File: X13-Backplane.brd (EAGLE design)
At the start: 101.6 x 139.3 mm, 38 parts, among them J1 PXC-PTSM-04-RA-1778641, J2 284512-4, J3 284512-8, J4 PXC-PTSM-04-RA-1778641, J5 PXC-PTSM-04-RA-1778641, J6 284512-4, J8 284512-8, T1 284512-3, T2 284512-3, T3 284512-3, T4 284512-3, T5 284512-3, T6 284512-3, T7 284512-3, T8 284512-3

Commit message: updated mux
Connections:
- removed net SWCLK_4: MUX.11
- removed net SWDIO_4: MUX.4
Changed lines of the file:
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@@
 <wire x1="15.08125" y1="51.435" x2="15.08125" y2="48.5648" width="0.2032" layer="1"/>
-</signal>
-<signal name="SWDIO_4">
-<contactref element="MUX" pad="4"/>
-</signal>
-<signal name="SWCLK_4">
-<contactref element="MUX" pad="11"/>
 </signal>
 <signal name="T1_PHS1">

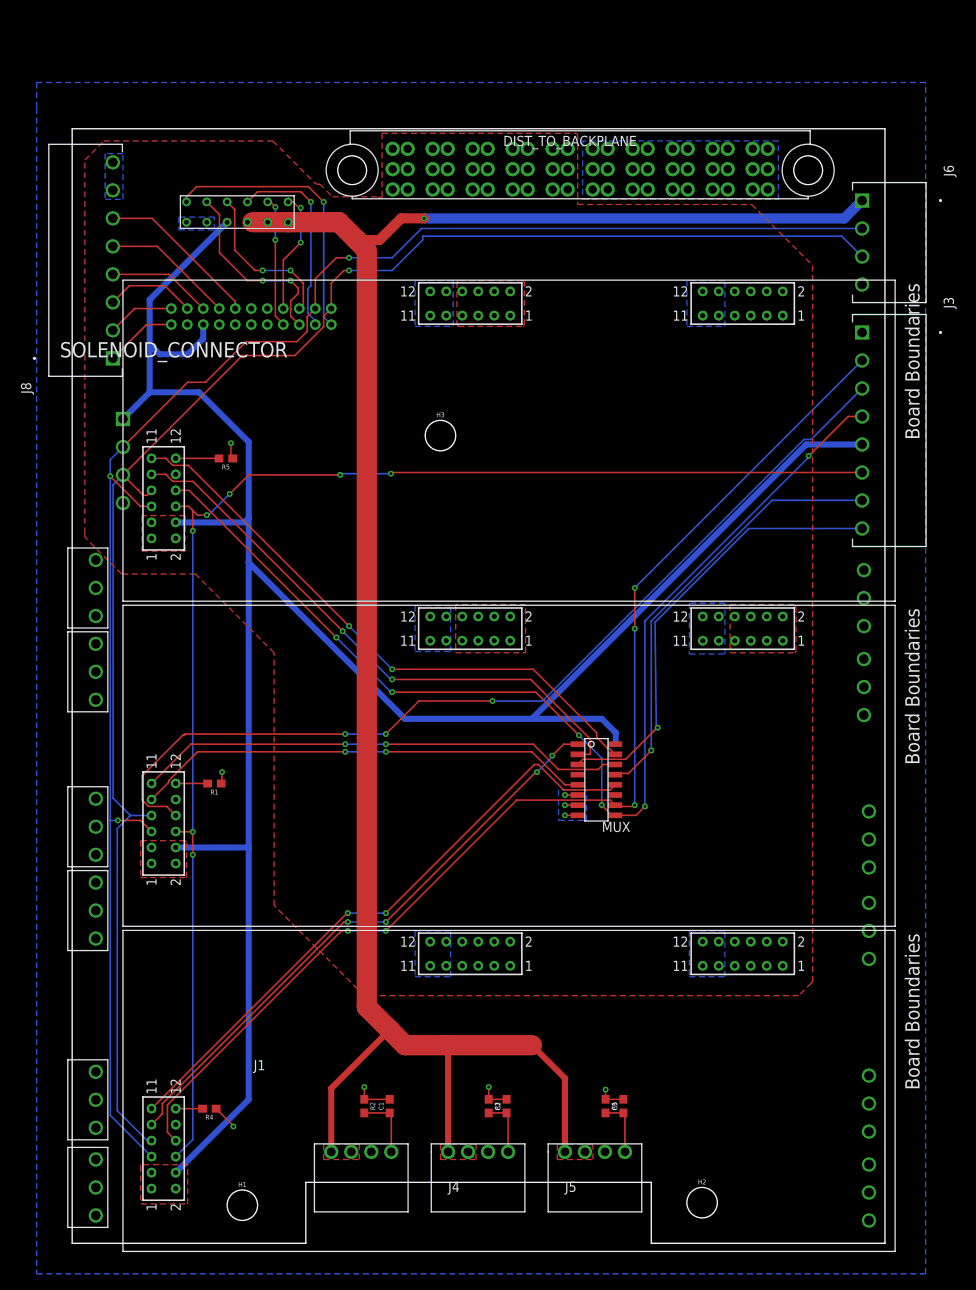
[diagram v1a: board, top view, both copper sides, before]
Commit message: updated 5v trace
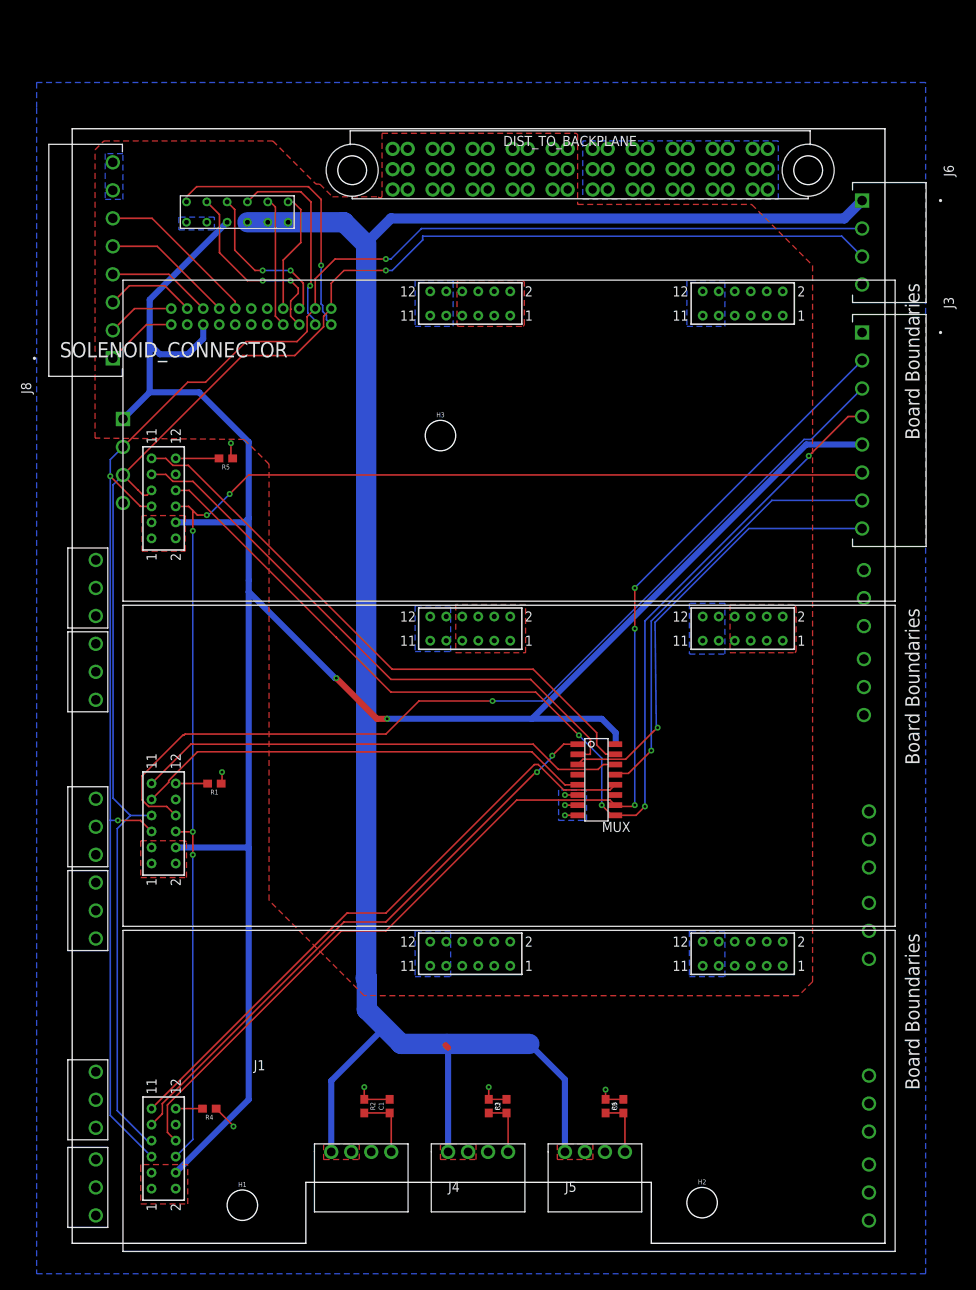
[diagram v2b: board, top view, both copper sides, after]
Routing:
- net 3.3V: track 279.8 -> 278.3 mm, vias 0 -> 2
- net SWCLK_3: track 73.6 -> 74.2 mm, vias 2 -> 0
- net C2_2: track 15.7 -> 15.3 mm, vias 2 -> 0
- net 5V: track 245.0 -> 244.8 mm, vias 1 -> 0
- net PROG_3: vias 6 -> 4
- net PROG_1: vias 5 -> 3
- net NRST: vias 7 -> 5
- net SWCLK_1: vias 2 -> 0
- net PROG_2: vias 3 -> 1
- net SWCLK_2: vias 2 -> 0
- net SWDIO_3: vias 2 -> 0
- net SWDIO_2: vias 2 -> 0
- net SWDIO_1: vias 4 -> 2
- net C2_1: vias 2 -> 0

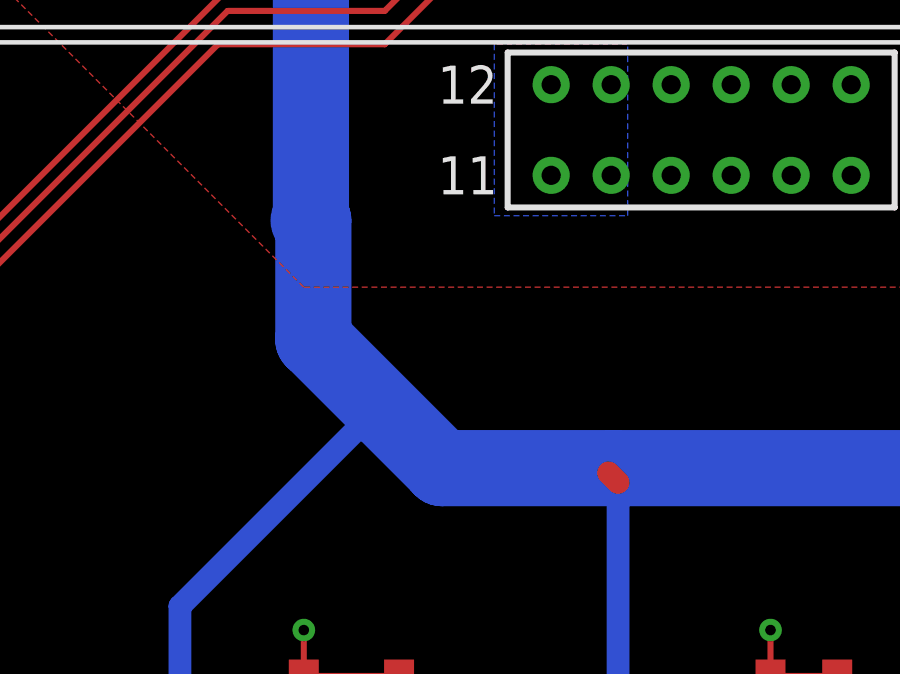
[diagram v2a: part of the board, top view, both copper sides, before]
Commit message: updated 5v trace
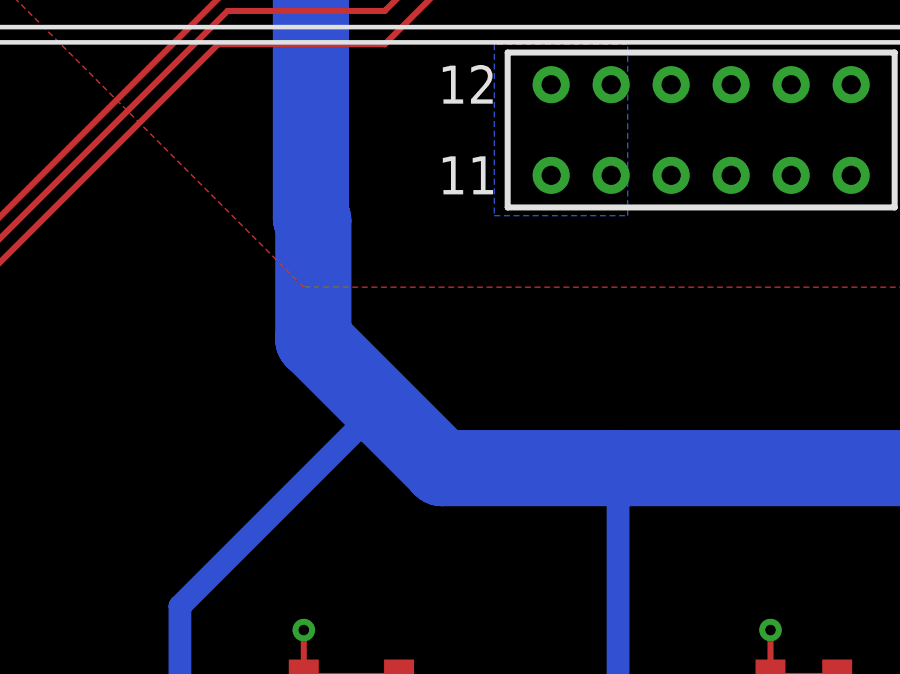
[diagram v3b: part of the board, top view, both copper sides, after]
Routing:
- net 5V: track 244.8 -> 244.2 mm
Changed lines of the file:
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@@
 <vertex x="65.0875" y="12.3825"/>
 </polygon>
-<wire x1="46.6725" y1="24.765" x2="46.99" y2="24.4475" width="0.762" layer="1"/>
 <wire x1="96.50875" y1="128.11125" x2="98.7425" y2="130.345" width="1.27" layer="16"/>
 <wire x1="21.9075" y1="127.635" x2="33.9725" y2="127.635" width="2.54" layer="16"/>
@@
 <wire x1="39.84625" y1="128.11125" x2="96.50875" y2="128.11125" width="1.27" layer="16"/>
 <wire x1="36.750625" y1="125.015625" x2="36.750625" y2="33.258125" width="2.54" layer="16"/>
-<wire x1="36.67125" y1="33.17875" x2="36.750625" y2="33.258125" width="2.54" layer="16"/>
 <wire x1="36.750625" y1="33.258125" x2="36.83" y2="33.17875" width="2.54" layer="16"/>
 <wire x1="36.83" y1="33.17875" x2="36.83" y2="29.21" width="2.54" layer="16"/>
@@
 <wire x1="24.4475" y1="127.635" x2="26.9875" y2="127.635" width="0" layer="19" extent="1-1"/>
 <wire x1="21.9075" y1="127.635" x2="24.4475" y2="127.635" width="0" layer="19" extent="1-1"/>
-<wire x1="38.25875" y1="26.19375" x2="36.67125" y2="33.17875" width="0" layer="19" extent="16-16"/>
-<wire x1="46.6725" y1="24.765" x2="38.25875" y2="26.19375" width="0" layer="19" extent="1-16"/>
+<wire x1="64.095" y1="11.43" x2="61.595" y2="11.43" width="0" layer="19" extent="1-1"/>
+<wire x1="49.49" y1="11.43" x2="46.99" y2="11.43" width="0" layer="19" extent="1-1"/>
+<wire x1="34.885" y1="11.43" x2="46.99" y2="11.43" width="0" layer="19" extent="1-1"/>
+<wire x1="32.385" y1="11.43" x2="34.885" y2="11.43" width="0" layer="19" extent="1-1"/>
 </signal>
 <signal name="12V">

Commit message: updated spacing on parts
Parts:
- moved MC2 1.91 mm to (100.8, 67.6)
- moved MC1 1.12 mm to (100.8, 79.5)
- moved T5 0.95 mm to (0.95, 40.6)
- moved T7 0.79 mm to (0.95, 70.6)
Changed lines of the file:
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@@
 <attribute name="VALUE" x="94.0925" y="118.3" size="1.27" layer="27" rot="R270"/>
 </element>
-<element name="MC1" library="ThrusterConnector" package="284512-3" value="284512-3" x="100.965" y="80.645" smashed="yes" rot="MR180"/>
-<element name="MC2" library="ThrusterConnector" package="284512-3" value="284512-3" x="100.965" y="69.5325" smashed="yes" rot="MR180"/>
+<element name="MC1" library="ThrusterConnector" package="284512-3" value="284512-3" x="100.80625" y="79.53375" smashed="yes" rot="MR180"/>
+<element name="MC2" library="ThrusterConnector" package="284512-3" value="284512-3" x="100.80625" y="67.6275" smashed="yes" rot="MR180"/>
 <element name="MC3" library="ThrusterConnector" package="284512-3" value="284512-3" x="101.6" y="50.4825" smashed="yes" rot="MR180"/>
 <element name="MC4" library="ThrusterConnector" package="284512-3" value="284512-3" x="101.6" y="39.0525" smashed="yes" rot="MR180"/>
@@
 <element name="T3" library="ThrusterConnector" package="284512-3" value="284512-3" x="0.9525" y="6.985" smashed="yes" rot="R180"/>
 <element name="T4" library="ThrusterConnector" package="284512-3" value="284512-3" x="0.9525" y="17.93875" smashed="yes" rot="R180"/>
-<element name="T5" library="ThrusterConnector" package="284512-3" value="284512-3" x="0.9525" y="41.5925" smashed="yes" rot="R180"/>
+<element name="T5" library="ThrusterConnector" package="284512-3" value="284512-3" x="0.9525" y="40.64" smashed="yes" rot="R180"/>
 <element name="T6" library="ThrusterConnector" package="284512-3" value="284512-3" x="0.9525" y="52.07" smashed="yes" rot="R180"/>
-<element name="T7" library="ThrusterConnector" package="284512-3" value="284512-3" x="0.9525" y="71.4375" smashed="yes" rot="R180"/>
+<element name="T7" library="ThrusterConnector" package="284512-3" value="284512-3" x="0.9525" y="70.64375" smashed="yes" rot="R180"/>
 <element name="T8" library="ThrusterConnector" package="284512-3" value="284512-3" x="0.9525" y="81.915" smashed="yes" rot="R180"/>
 <element name="J1" library="Phoenix Contact PTSM-04-V-1778573" package="PXC-PTSM-04-RA-1778641" value="PXC-PTSM-04-RA-1778641" x="32.385" y="11.43" smashed="yes">

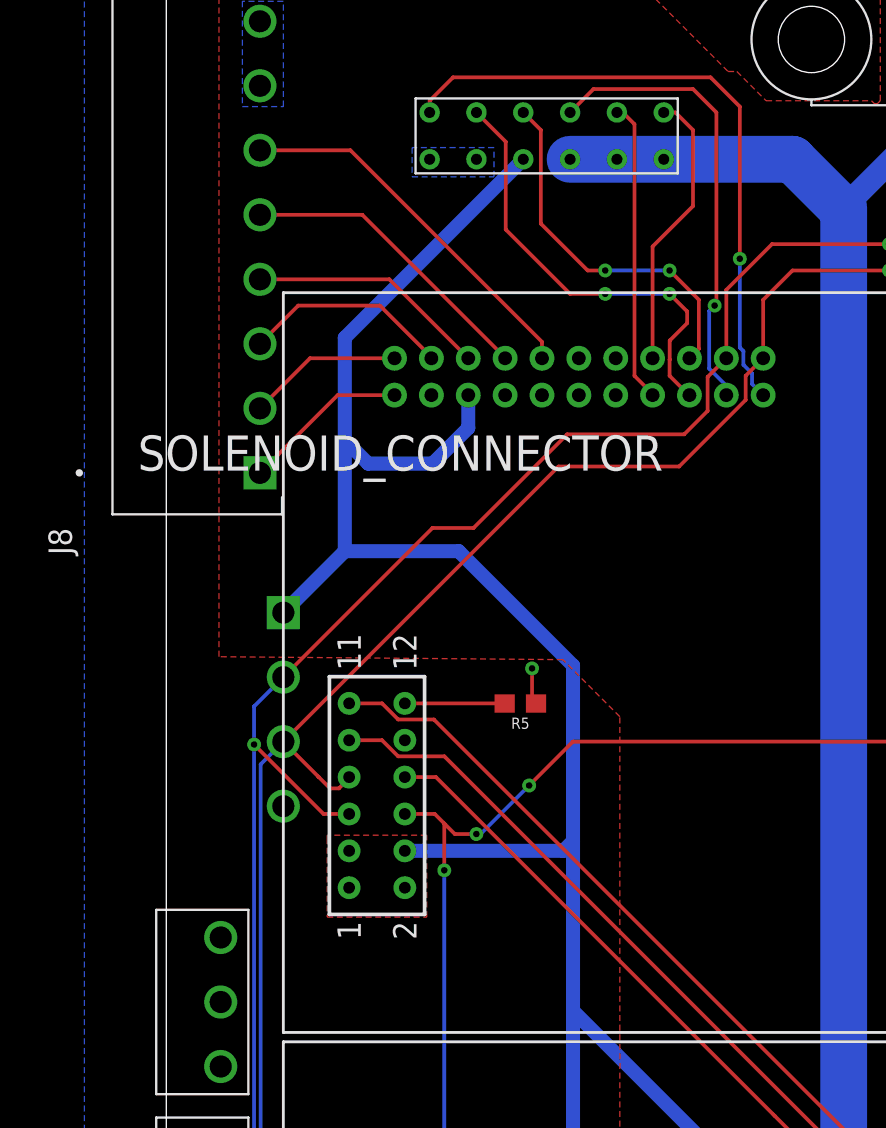
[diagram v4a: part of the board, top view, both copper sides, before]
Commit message: Placed Solenoid Connector and schematic pinout
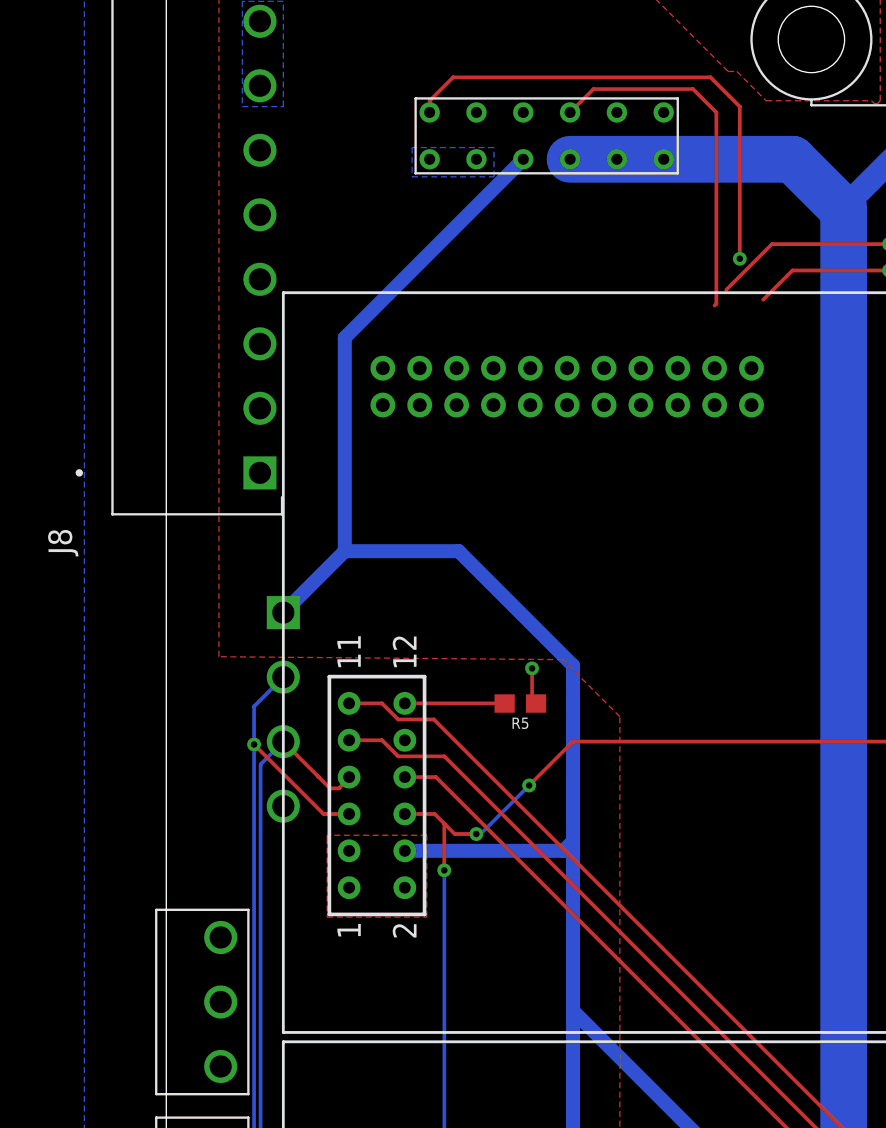
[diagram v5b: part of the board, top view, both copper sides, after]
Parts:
- removed SOLENOID_CONNECTOR: BKP-TO-SOL, Solenoid Connector (backplane side):BKP-TO-SOL_TMM-111-01-T-D
- added U$4: BKP-TO-SOL, Solenoid Connector (backplane side):BKP-TO-SOL_TMM-111-01-T-D
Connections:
- new net DATA1: U$4.22
- net 12V: now also U$4.11; no longer SOLENOID_CONNECTOR.11
- net 3.3V: now also U$4.4; no longer SOLENOID_CONNECTOR.6
- net ALERT_1: now also U$4.18; no longer SOLENOID_CONNECTOR.18
- net ALERT_2: now also U$4.17; no longer SOLENOID_CONNECTOR.17
- net C2_1: now also U$4.16; no longer SOLENOID_CONNECTOR.16
- net C2_2: now also U$4.15; no longer SOLENOID_CONNECTOR.15
- net CAN_H: now also U$4.19; no longer SOLENOID_CONNECTOR.19
- net CAN_L: now also U$4.21; no longer SOLENOID_CONNECTOR.21
- net CLK: now also U$4.20; no longer SOLENOID_CONNECTOR.20
- net DATA: no longer SOLENOID_CONNECTOR.22
- net GND: now also U$4.10, U$4.12, U$4.6, U$4.8; no longer SOLENOID_CONNECTOR.10, SOLENOID_CONNECTOR.12, SOLENOID_CONNECTOR.4, SOLENOID_CONNECTOR.8
- net MC1_PHS1: now also MC1.1; no longer MC1.P$1
- net MC1_PHS2: now also MC1.2; no longer MC1.P$2
- net MC1_PHS3: now also MC1.3; no longer MC1.P$3
- net MC2_PHS1: now also MC2.1; no longer MC2.P$1
- net MC2_PHS2: now also MC2.2; no longer MC2.P$2
- net MC2_PHS3: now also MC2.3; no longer MC2.P$3
- net MC3_PHS1: now also MC3.1; no longer MC3.P$1
- net MC3_PHS2: now also MC3.2; no longer MC3.P$2
- net MC3_PHS3: now also MC3.3; no longer MC3.P$3
- net MC4_PHS1: now also MC4.1; no longer MC4.P$1
- net MC4_PHS2: now also MC4.2; no longer MC4.P$2
- net MC4_PHS3: now also MC4.3; no longer MC4.P$3
- net NRST: now also U$4.13
- net SOL1_1: now also U$4.2; no longer SOLENOID_CONNECTOR.2
- net SOL2_1: now also U$4.1; no longer SOLENOID_CONNECTOR.1
- net SOL3_1: now also U$4.3; no longer SOLENOID_CONNECTOR.3
- net SOL4_1: now also U$4.5; no longer SOLENOID_CONNECTOR.5
- net SOL5_1: now also U$4.7; no longer SOLENOID_CONNECTOR.7
- net SOL6_1: now also U$4.9; no longer SOLENOID_CONNECTOR.9
- net T1_PHS1: now also T1.1; no longer T1.P$1
- net T1_PHS2: now also T1.2; no longer T1.P$2
- net T1_PHS3: now also T1.3; no longer T1.P$3
- net T2_PHS1: now also T2.1; no longer T2.P$1
- net T2_PHS2: now also T2.2; no longer T2.P$2
- net T2_PHS3: now also T2.3; no longer T2.P$3
- net T3_PHS1: now also T3.1; no longer T3.P$1
- net T3_PHS2: now also T3.2; no longer T3.P$2
- net T3_PHS3: now also T3.3; no longer T3.P$3
- net T4_PHS1: now also T4.1; no longer T4.P$1
- net T4_PHS2: now also T4.2; no longer T4.P$2
- net T4_PHS3: now also T4.3; no longer T4.P$3
- net T5_PHS1: now also T5.1; no longer T5.P$1
- net T5_PHS2: now also T5.2; no longer T5.P$2
- net T5_PHS3: now also T5.3; no longer T5.P$3
- net T6_PHS1: now also T6.1; no longer T6.P$1
- net T6_PHS2: now also T6.2; no longer T6.P$2
- net T6_PHS3: now also T6.3; no longer T6.P$3
- net T7_PHS1: now also T7.1; no longer T7.P$1
- net T7_PHS2: now also T7.2; no longer T7.P$2
- net T7_PHS3: now also T7.3; no longer T7.P$3
- net T8_PHS1: now also T8.1; no longer T8.P$1
- net T8_PHS2: now also T8.2; no longer T8.P$2
- net T8_PHS3: now also T8.3; no longer T8.P$3
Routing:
- net CAN_L: track 203.7 -> 165.1 mm
- net CAN_H: track 210.9 -> 175.0 mm
- net ALERT_1: track 24.1 -> 0.00 mm, vias 2 -> 0
- net SOL6_1: track 20.5 -> 0.00 mm
- net ALERT_2: track 20.1 -> 0.00 mm, vias 2 -> 0
- net SOL5_1: track 16.5 -> 0.00 mm
- net C2_1: track 16.3 -> 0.00 mm
- net C2_2: track 15.3 -> 0.00 mm
- net SOL4_1: track 13.1 -> 0.00 mm
- net SOL3_1: track 11.4 -> 0.00 mm
- net 3.3V: track 278.3 -> 268.5 mm
- net SOL1_1: track 9.05 -> 0.00 mm
- net SOL2_1: track 8.43 -> 0.00 mm
- net DATA: track 34.8 -> 26.9 mm
- net CLK: track 24.9 -> 19.5 mm, vias 1 -> 0
